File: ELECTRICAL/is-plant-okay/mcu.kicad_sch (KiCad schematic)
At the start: 1 part

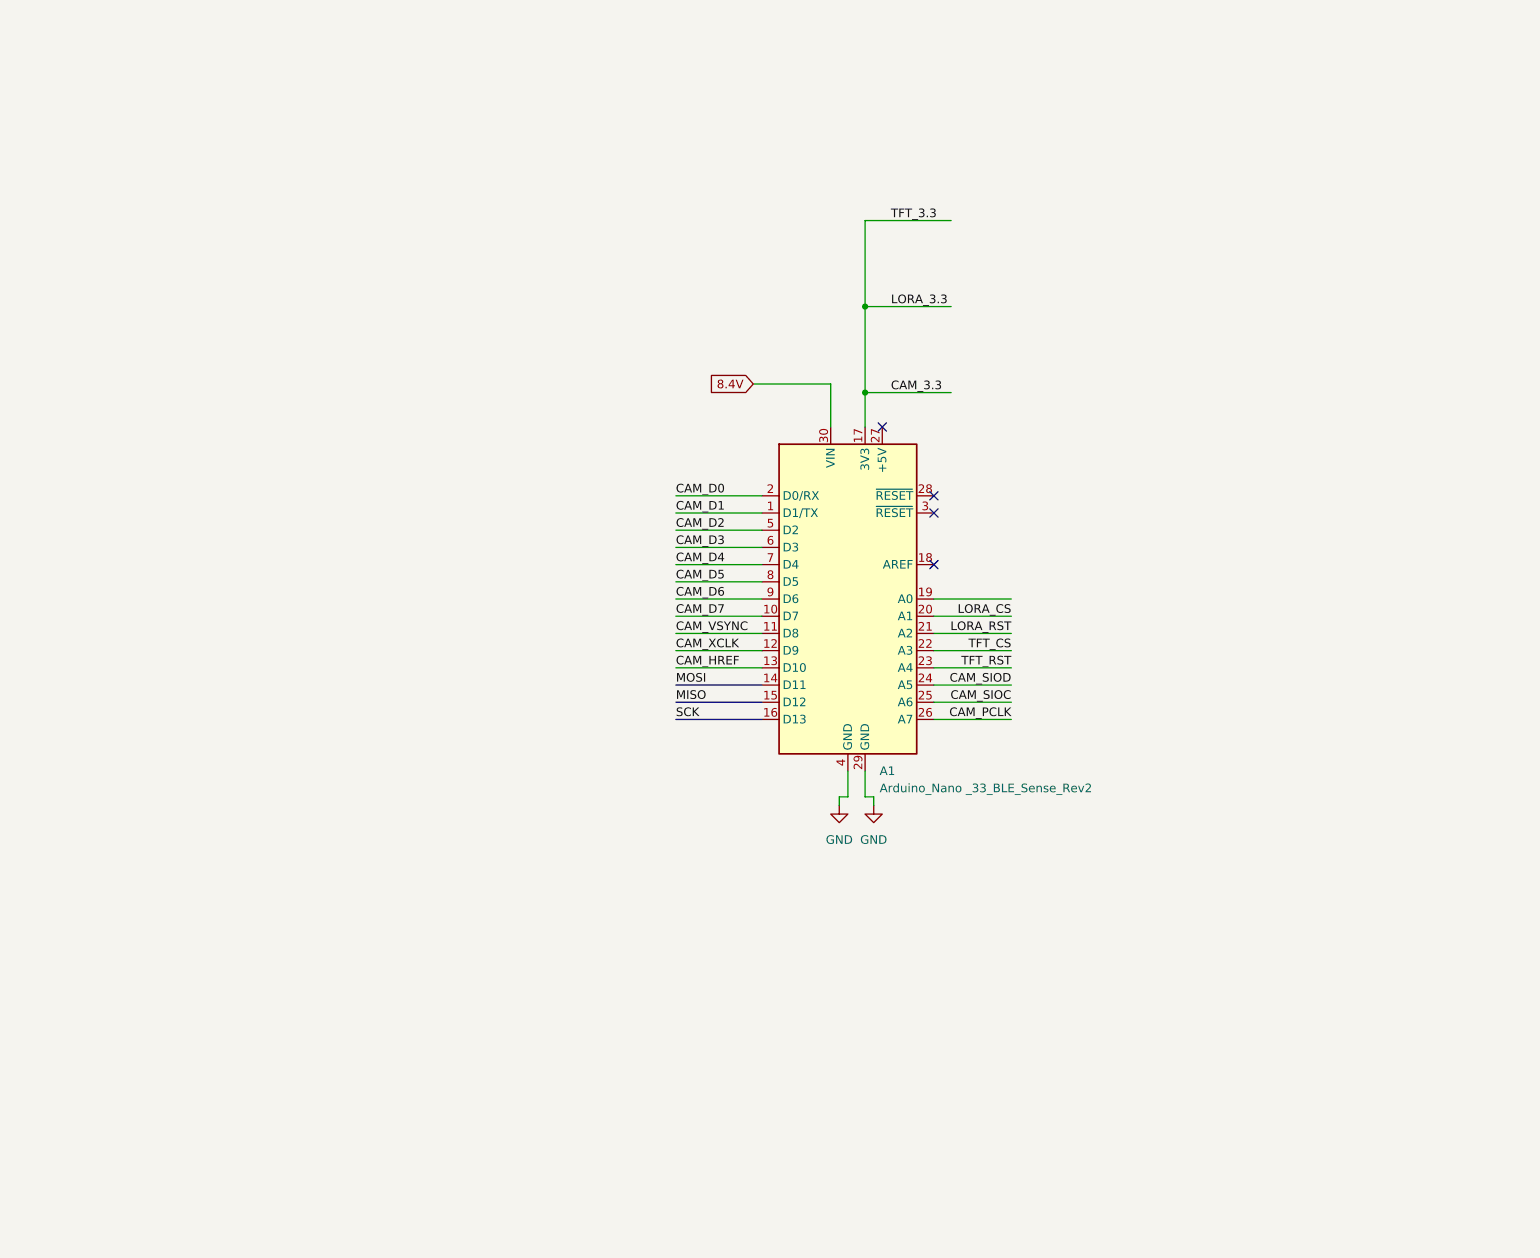
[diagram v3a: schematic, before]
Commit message: feat: minor pin fixes, add camera moduel to schematic
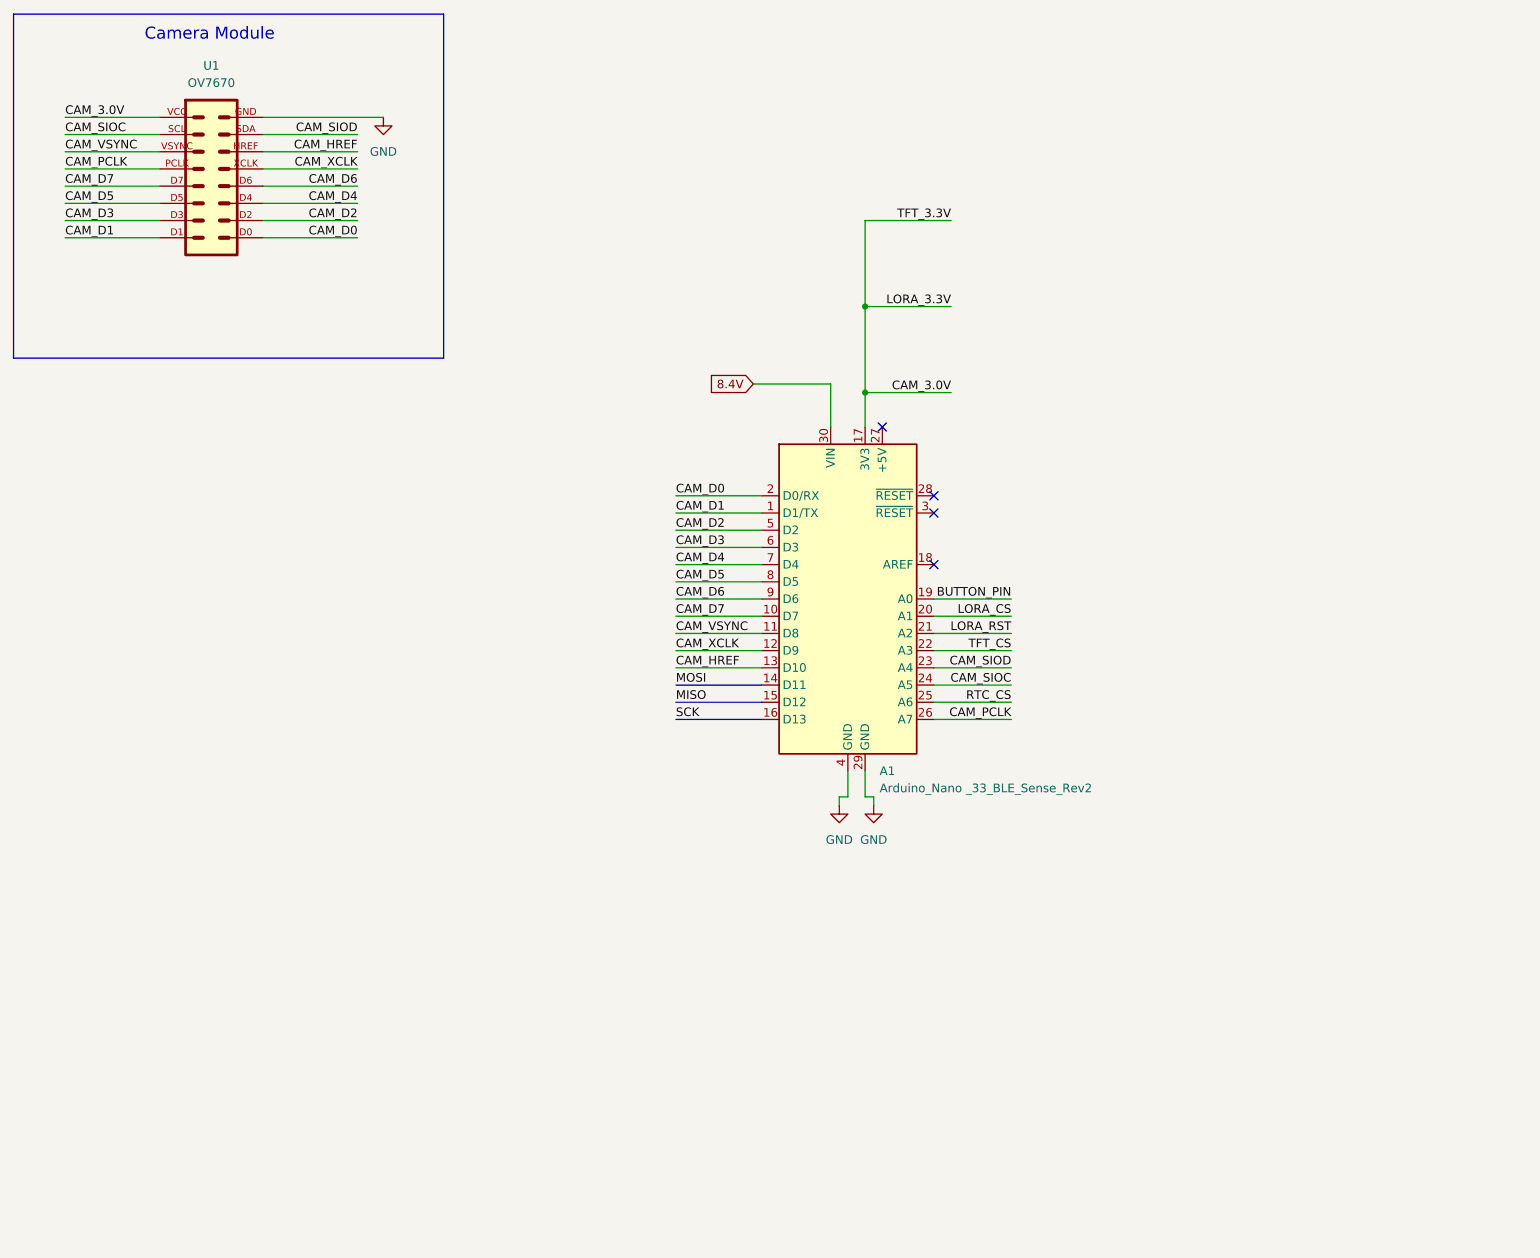
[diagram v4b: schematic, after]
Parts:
- added U1: OV7670, OV7670:OV7670, symbol is-plant-okay-lib:OV7670
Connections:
- net TFT_RST is gone; now on net CAM_SIOD: A1.23 (A4)
- net CAM_D0: now also U1.D0
- net CAM_D1: now also U1.D1
- net CAM_D2: now also U1.D2
- net CAM_D3: now also U1.D3
- net CAM_D4: now also U1.D4
- net CAM_D5: now also U1.D5
- net CAM_D6: now also U1.D6
- net CAM_D7: now also U1.D7
- net CAM_HREF: now also U1.HREF
- net CAM_PCLK: now also U1.PCLK
- net CAM_SIOC: now also A1.24 (A5), U1.SCL; no longer A1.25 (A6)
- net CAM_SIOD: now also U1.SDA; no longer A1.24 (A5)
- net CAM_VSYNC: now also U1.VSYNC
- net CAM_XCLK: now also U1.XCLK
- net GND: now also U1.GND
- net BUTTON_PIN: now reaches A1.19 (A0)
- net CAM_3.3 renamed CAM_3.0V
- net CAM_3.0V: now also U1.VCC
- new net RTC_CS: A1.25 (A6)
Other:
- note added: "Camera Module"

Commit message: feat: add lora, rtc, coin cell, tft screen to schematic
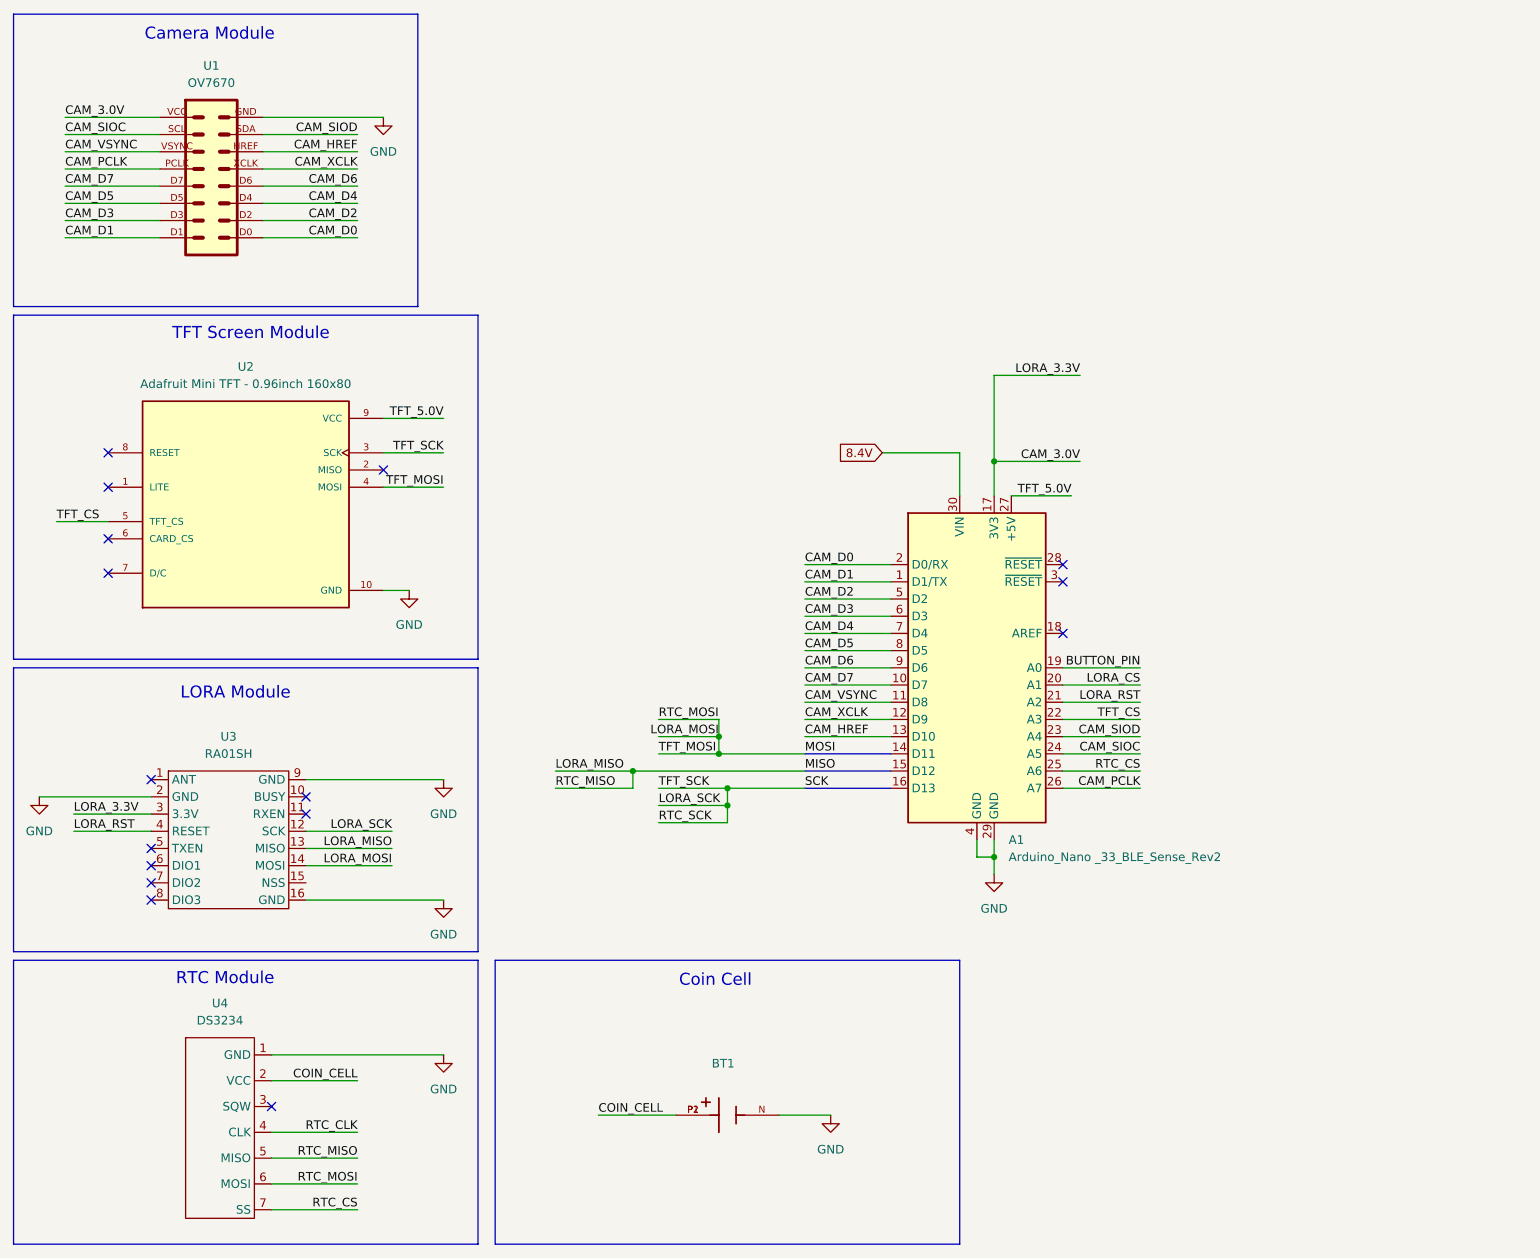
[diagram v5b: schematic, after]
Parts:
- added BT1: ~, Custom_Library:BAT_3034, symbol CustomLibrary:3034
- added U2: Adafruit Mini TFT - 0.96inch 160x80, 358:MODULE_358, symbol is-plant-okay-lib:358
- added U3: RA01SH, symbol is-plant-okay-lib:RA-01SH
- added U4: DS3234, symbol is-plant-okay-lib:DS3234
- A1, U1: now left out of the parts list
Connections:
- net CAM_3.0V: now also U3.3 (3.3V)
- net GND: now also BT1.N, U2.10 (GND), U3.16 (GND), U3.2 (GND), U3.9 (GND), U4.1 (GND)
- net LORA_RST: now also U3.4 (RESET)
- net RTC_CS: now also U4.7 (SS)
- net TFT_CS: now also U2.5 (TFT_CS)
- net TFT_5.0V: now reaches A1.27 (+5V)
- net TFT_5.0V: now also U2.9 (VCC)
- new net COIN_CELL: BT1.P1, BT1.P2, U4.2 (VCC)
- new net LORA_MISO: U3.13 (MISO), U4.5 (MISO)
- new net LORA_MOSI: U2.4 (MOSI), U3.14 (MOSI), U4.6 (MOSI)
- new net LORA_SCK: U2.3 (SCK), U3.12 (SCK)
- new net RTC_CLK: U4.4 (CLK)
- no-connect marks 4 -> 16
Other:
- note added: "Coin Cell"
- note added: "LORA Module"
- note added: "RTC Module"
- note added: "TFT Screen Module"
- moved on the sheet: A1

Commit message: feat: add pins to setup function
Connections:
- net TFT_5.0V: no longer A1.27 (+5V)
- no-connect marks 16 -> 17
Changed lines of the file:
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@@
+	)
+	(junction
+		(at 157.48 72.39)
+		(diameter 0)
+		(color 0 0 0 0)
 	)
 	(junction
@@
 	)
 	(no_connect
+		(at 160.02 83.82)
+	)
+	(no_connect
 		(at 26.67 90.17)
 	)
@@
 	(wire
 		(pts
+			(xy 157.48 72.39) (xy 157.48 78.74)
+		)
+		(stroke
+			(width 0)
+			(type default)
+		)
+	)
+	(wire
+		(pts
 			(xy 55.88 133.35) (xy 68.58 133.35)
 		)
@@
 	(wire
 		(pts
-			(xy 157.48 66.04) (xy 157.48 78.74)
+			(xy 157.48 66.04) (xy 157.48 72.39)
 		)
 		(stroke
@@
 	(wire
 		(pts
-			(xy 160.02 83.82) (xy 168.91 83.82)
-		)
-		(stroke
-			(width 0)
-			(type default)
-		)
-	)
-	(wire
-		(pts
 			(xy 129.54 99.06) (xy 142.24 99.06)
 		)
@@
 		(pts
 			(xy 107.95 116.84) (xy 116.84 116.84)
+		)
+		(stroke
+			(width 0)
+			(type default)
+		)
+	)
+	(wire
+		(pts
+			(xy 170.18 72.39) (xy 157.48 72.39)
 		)
 		(stroke
@@
 		)
 	)
+	(label "TFT_3.3V"
+		(at 170.18 72.39 180)
+		(effects
+			(font
+				(size 1.27 1.27)
+			)
+			(justify right bottom)
+		)
+	)
 	(label "RTC_MOSI"
 		(at 63.5 185.42 180)
@@
 		(effects
 			(font
-				(size 1.27 1.27)
-			)
-			(justify right bottom)
-		)
-	)
-	(label "TFT_5.0V"
-		(at 168.91 83.82 180)
-		(effects
-			(font
